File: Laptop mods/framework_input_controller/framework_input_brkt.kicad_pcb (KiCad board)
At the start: 2 copper layers, 35 x 38.2 mm, 76 parts, among them J1 mobo_input_conn, J2 USB_C_Receptacle_USB2.0, J3 USBa, J4 USBb, J5 USB1, J6 USB0, J7 BOOT, J8 SWD, Q1 Q_NPN_BCE, Q2 Q_PMOS_GSD, U1 SL2.1A, U2 AP1117-33, U3 W25Q32JVSS, U4 RP2040, U5 74HC595, Y1 12MHz, Y2 12MHz, Y3 12MHz

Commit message: framework_input_controlled: forgot a few changes in the PCB
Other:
- board text added: "USB-C 2.0 (detachable!)"
- board text added: "v1 FrmW input cover controller by CRImier"
- board text removed: "USB-C 2.0"
- board text removed: "v1 FrmW input board controller by CRImier"
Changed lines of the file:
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@@
     (descr "Through hole straight pin header, 1x04, 2.54mm pitch, single row")
     (tags "Through hole pin header THT 1x04 2.54mm single row")
-    (fp_text reference J6 (at 1.785 0.06 180) (layer F.SilkS)
+    (fp_text reference J6 (at 1.785 0.56 180) (layer F.SilkS)
       (effects (font (size 1 1) (thickness 0.15)))
     )
@@
     (descr "Through hole straight pin header, 1x04, 2.54mm pitch, single row")
     (tags "Through hole pin header THT 1x04 2.54mm single row")
-    (fp_text reference J4 (at 0 -2.33) (layer F.SilkS)
+    (fp_text reference J4 (at 2.35 8.25) (layer F.SilkS)
       (effects (font (size 1 1) (thickness 0.15)))
     )
@@
     (effects (font (size 1 1) (thickness 0.15)) (justify right mirror))
   )
-  (gr_text "USB-C 2.0" (at 143.525 103.225) (layer F.SilkS)
+  (gr_text "USB-C 2.0 (detachable!)" (at 143.525 103.225) (layer F.SilkS)
     (effects (font (size 0.8 0.8) (thickness 0.13)) (justify left))
   )
@@
     (effects (font (size 0.8 0.8) (thickness 0.13)) (justify left))
   )
-  (gr_text "USB hub (or not)" (at 161.2 113.775 90) (layer F.SilkS)
+  (gr_text "USB hub (or not)" (at 161.2 113 90) (layer F.SilkS)
     (effects (font (size 0.8 0.8) (thickness 0.13)) (justify left))
   )
@@
     (effects (font (size 0.8 0.8) (thickness 0.13)) (justify left))
   )
-  (gr_text "v1  FrmW\ninput board controller by CRImier" (at 176 101.6 90) (layer F.SilkS)
+  (gr_text "v1  FrmW\ninput cover controller by CRImier" (at 176 101.6 90) (layer F.SilkS)
     (effects (font (size 0.95 0.95) (thickness 0.15)) (justify left))
   )

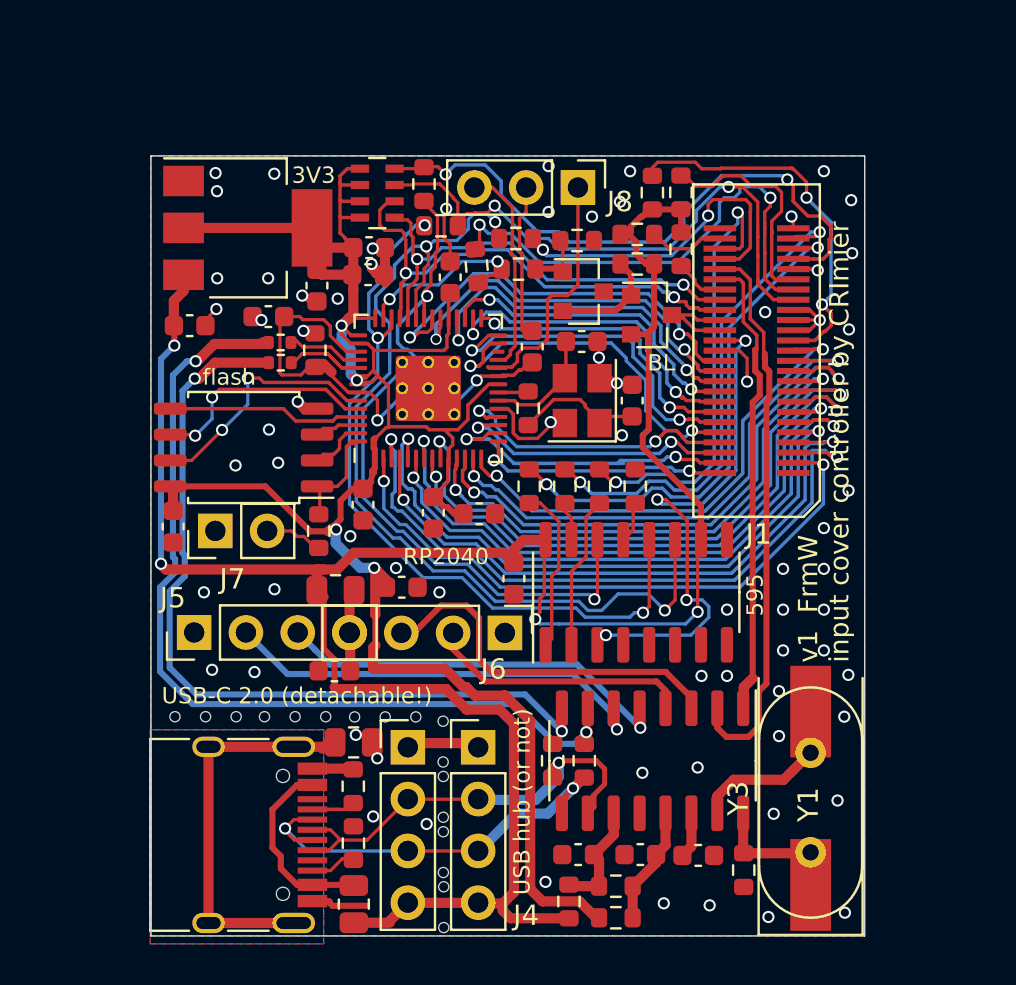
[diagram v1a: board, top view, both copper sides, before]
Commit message: framework_input_controller: adding fiducials, rerouting a few tracks, tweaking silk, adding silk clarifications and warnings
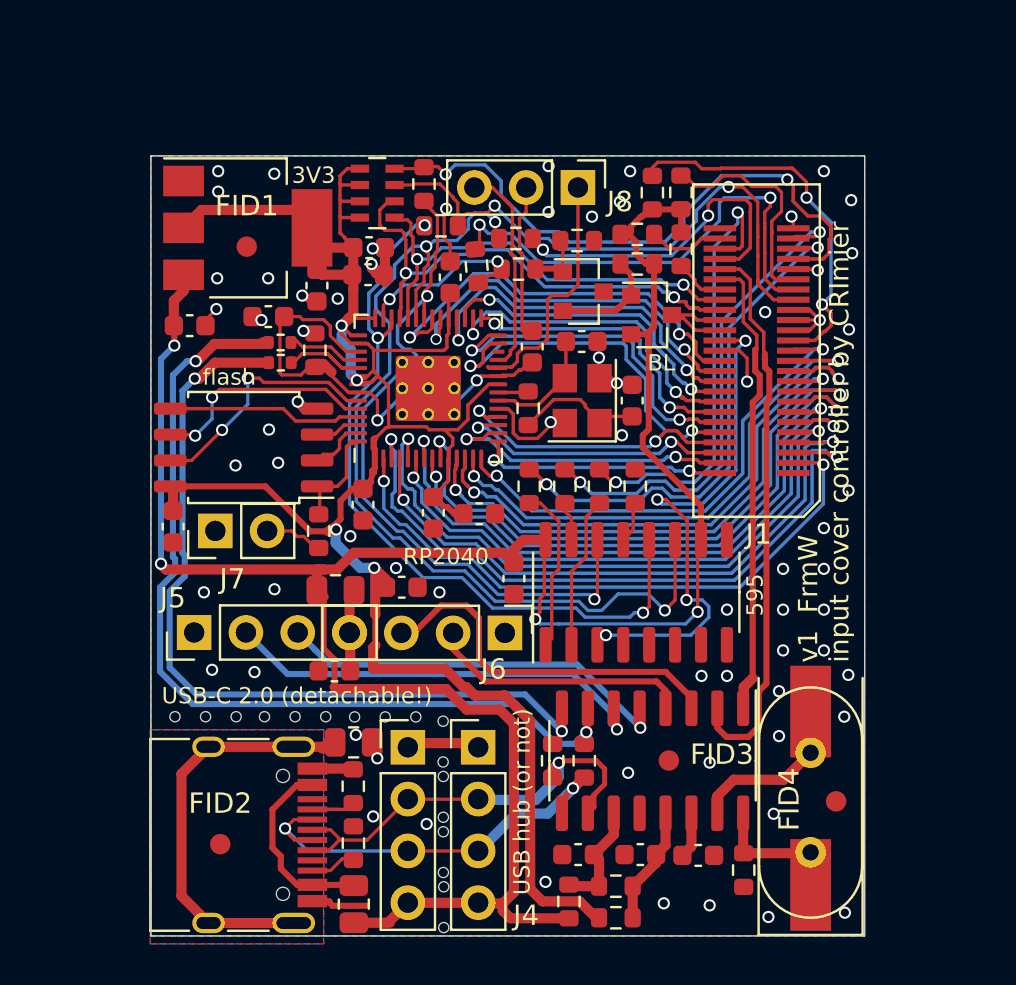
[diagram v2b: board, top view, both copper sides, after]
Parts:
- added FID1: Fiducial, Fiducial:Fiducial_1mm_Mask2mm, F.Cu at (147.7, 81.2)
- added FID2: Fiducial, Fiducial:Fiducial_1mm_Mask2mm, F.Cu at (146.4, 110.5)
- added FID3: Fiducial, Fiducial:Fiducial_1mm_Mask2mm, F.Cu at (168.4, 106.4)
- added FID4: Fiducial, Fiducial:Fiducial_1mm_Mask2mm, F.Cu at (176.6, 108.4)
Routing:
- net /SHD: track 19.3 -> 20.4 mm
- net +3V3: track 108.1 -> 108.8 mm
- net /TP_BOARD_ID: track 25.2 -> 24.6 mm
- net GND: vias 70 -> 69
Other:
- board text added: "==>"
- board text added: "I spent 13 hours on this one - treat it well!"
- board text added: "There is only one right way to insert the input FPC: so that it is directed away from the edge, like this: The other way, lies destruction."
- board text added: "careful snapping this off! first, this side =>"
- board text removed: "I spent 12 hours on this one - treat it well!"

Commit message: framework_input_controller: moved to KiCad 6
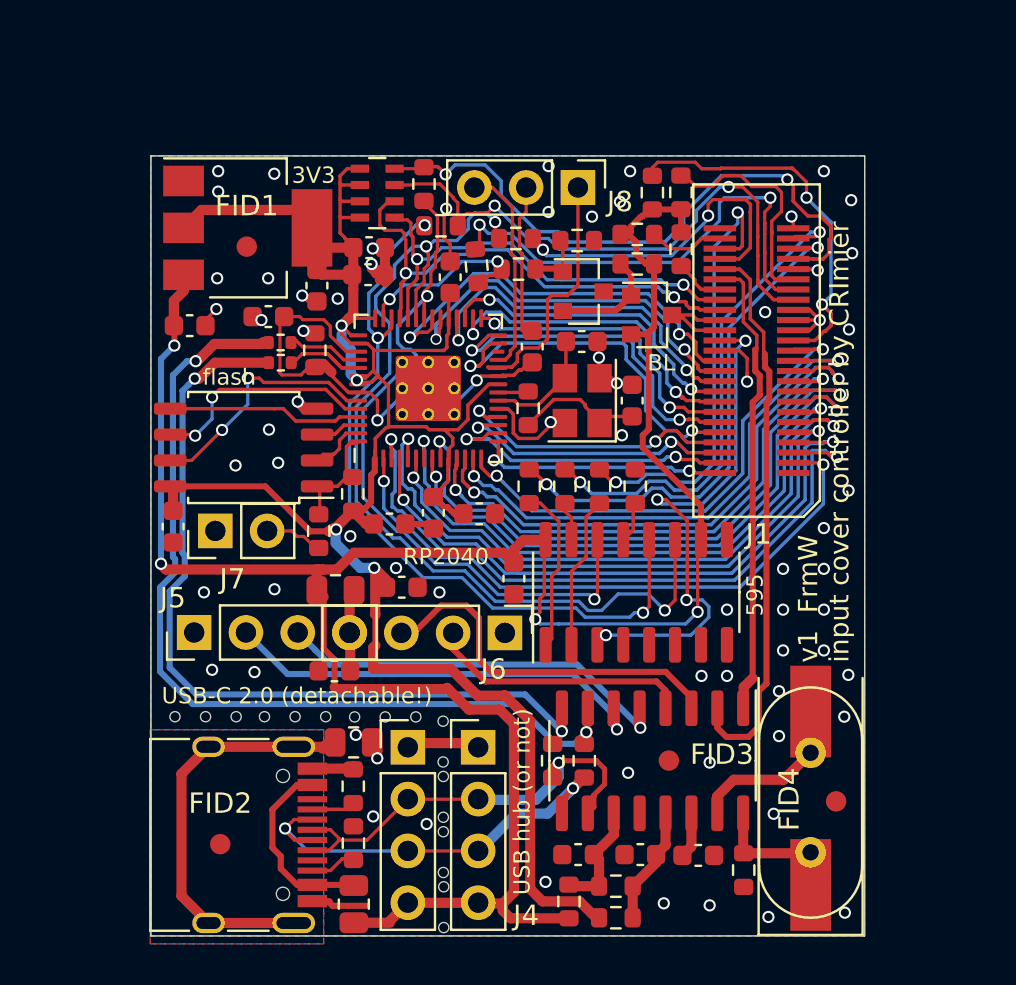
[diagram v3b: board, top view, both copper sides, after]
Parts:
- added R31: 10K, Resistor_SMD:R_0603_1608Metric, F.Cu at (152.9, 93.3)
- moved C10 1.61 mm to (154.7, 94.8), turned to 0 degrees
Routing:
- net +3V3: track 108.8 -> 107.2 mm
- net GND: track 42.2 -> 43.7 mm
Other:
- net class Default removed

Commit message: framework_input_controller: v2, routing fixes, PCBA optimization, small updates and bugfixes
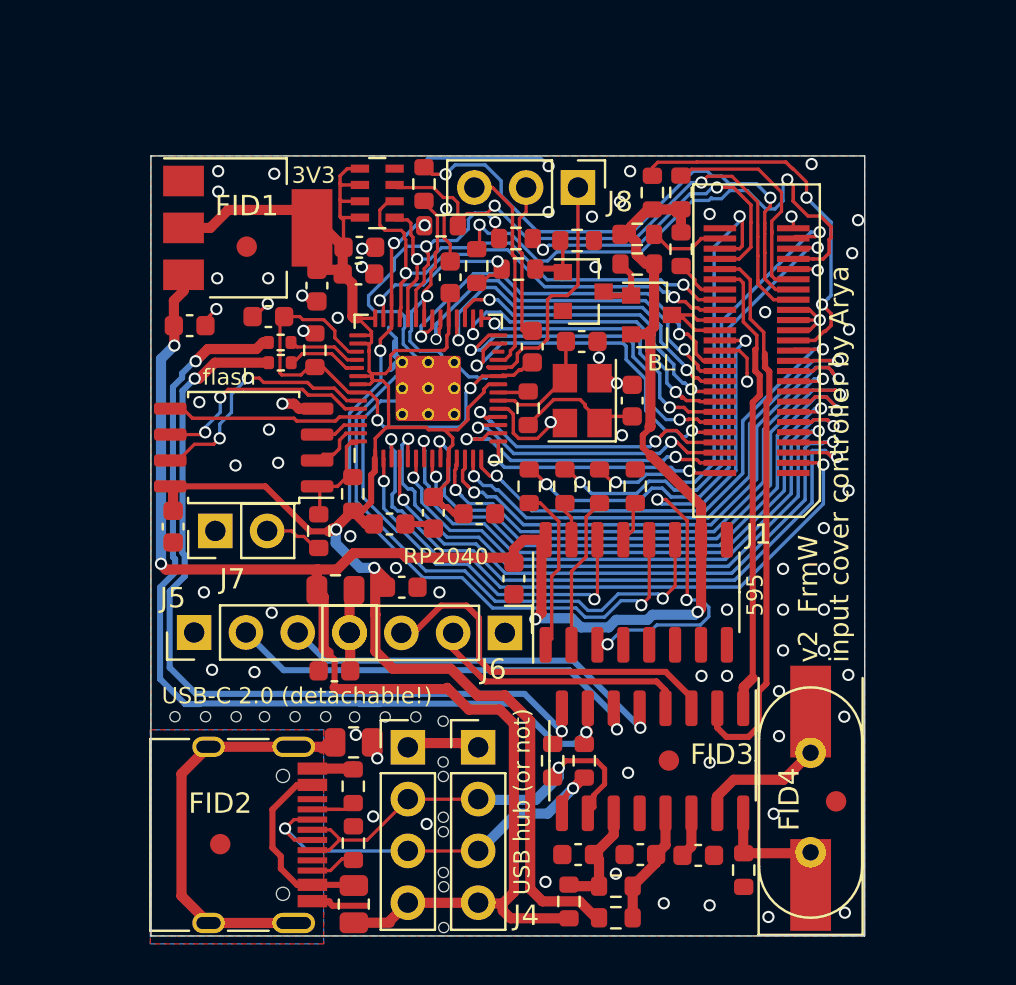
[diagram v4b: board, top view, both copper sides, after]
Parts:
- C12, C16: value 100nF -> 1uF
- C19, C20: value Cc -> 18pF
- Q1: value Q_NPN_BCE -> BC817
- Q2: value Q_PMOS_GSD -> CJ2305
- R10, R11: value NC -> 0R
- R13, R2: value 0R/F -> 0R
- R30: value 0R -> FB
- R31: value 10K -> 5K1
- RN2: value 10K -> 4.7K
- moved C12 0.48 mm to (153.2, 81.2)
- moved C13 0.47 mm to (153.2, 82.5)
- turned R18 to 90 degrees
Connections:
- J1 pad 26: Net-(J1-Pad26) -> unconnected-(J1-Pin_26-Pad26)
- J2 pad A8: Net-(J2-PadA8) -> unconnected-(J2-SBU1-PadA8)
- J2 pad B8: Net-(J2-PadB8) -> unconnected-(J2-SBU2-PadB8)
- Q1 pad 2: Net-(Q1-Pad2) -> GND
- Q1 pad 3: GND -> Net-(Q1-C)
- Q2 pad 1: Net-(Q1-Pad2) -> Net-(Q1-C)
- R15 pad 2: /FPR_CTRL -> /TP_BOARD_ID
- R18 pad 2: /TP_BOARD_ID -> /FPR_CTRL
- R22 pad 1: Net-(Q1-Pad2) -> Net-(Q1-C)
- RN2 pad 8: /FPR_CTRL -> unconnected-(RN2-R1.2-Pad8)
- U4 pad 26: Net-(U4-Pad26) -> unconnected-(U4-RUN-Pad26)
- U5 pad 4: Net-(U5-Pad4) -> unconnected-(U5-QE-Pad4)
- U5 pad 5: Net-(U5-Pad5) -> unconnected-(U5-QF-Pad5)
- U5 pad 6: Net-(U5-Pad6) -> unconnected-(U5-QG-Pad6)
- U5 pad 7: Net-(U5-Pad7) -> unconnected-(U5-QH-Pad7)
- U5 pad 9: Net-(U5-Pad9) -> unconnected-(U5-QH'-Pad9)
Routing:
- net GND: track 43.7 -> 61.5 mm, vias 69 -> 73
- net Net-(Q1-Pad2): track 5.43 -> 0.00 mm
- net +3V3: track 107.2 -> 103.3 mm, vias 4 -> 2
- net +5V: track 109.9 -> 113.5 mm
- net /FPR_CTRL: track 30.7 -> 27.4 mm
- net Net-(Q1-C): track 0.00 -> 3.20 mm
- net /TP_BOARD_ID: track 24.6 -> 26.9 mm
- net /595_DAT: track 35.6 -> 37.7 mm
- net /595_CLK: track 45.8 -> 47.6 mm
- net Net-(U4-USB_DP): track 5.08 -> 3.80 mm
- net /595_LAT: track 37.7 -> 36.6 mm, vias 3 -> 4
- net /KSO14: track 21.2 -> 20.5 mm
- net /KSO0: track 18.2 -> 17.6 mm
- net /FPR_LED_W: track 22.4 -> 21.9 mm
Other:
- board text added: "FrameWork laptop input board controller by Arya, v2"
- board text added: "I've spent 16 hours on this one - treat it well!"
- board text added: "careful snapping this off! first, this side >"
- board text added: "something secret steers us, but we still have to hold the gas pedal."
- board text added: "v2 FrmW input cover controller by Arya"
- board text removed: "FrameWork laptop input board controller by CRImier, v1"
- board text removed: "I spent 13 hours on this one - treat it well!"
- board text removed: "Looking in the mirror, she wrote in red: "I won't let myself become a distraction.""
- board text removed: "careful snapping this off! first, this side =>"
- board text removed: "v1 FrmW input cover controller by CRImier"

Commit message: framework_input_controller: iirc latest version as produced, changes not known
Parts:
- added H1: MountingHole, MountingHole:MountingHole_3mm, F.Cu at (140.0, 79.1)
- added H2: MountingHole, MountingHole:MountingHole_3mm, F.Cu at (181.0, 112.6)
- added Y4: 12MHz, Crystal:Crystal_SMD_3225-4Pin_3.2x2.5mm, F.Cu at (175.3, 108.5)
- moved FID4 14.7 mm to (166.7, 97.6)
- moved FID3 2.00 mm to (166.4, 106.4)
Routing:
- net /595_LAT: track 36.6 -> 37.5 mm
- net Net-(U1-XOUT): track 6.30 -> 7.16 mm
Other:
- board size 35 x 38.2 mm -> 45.8 x 38.2 mm
- rule pad_to_mask_clearance: 0.051 -> 0
- board text added: "trans rights!"
